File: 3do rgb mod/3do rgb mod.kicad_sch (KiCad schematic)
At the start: 12 parts

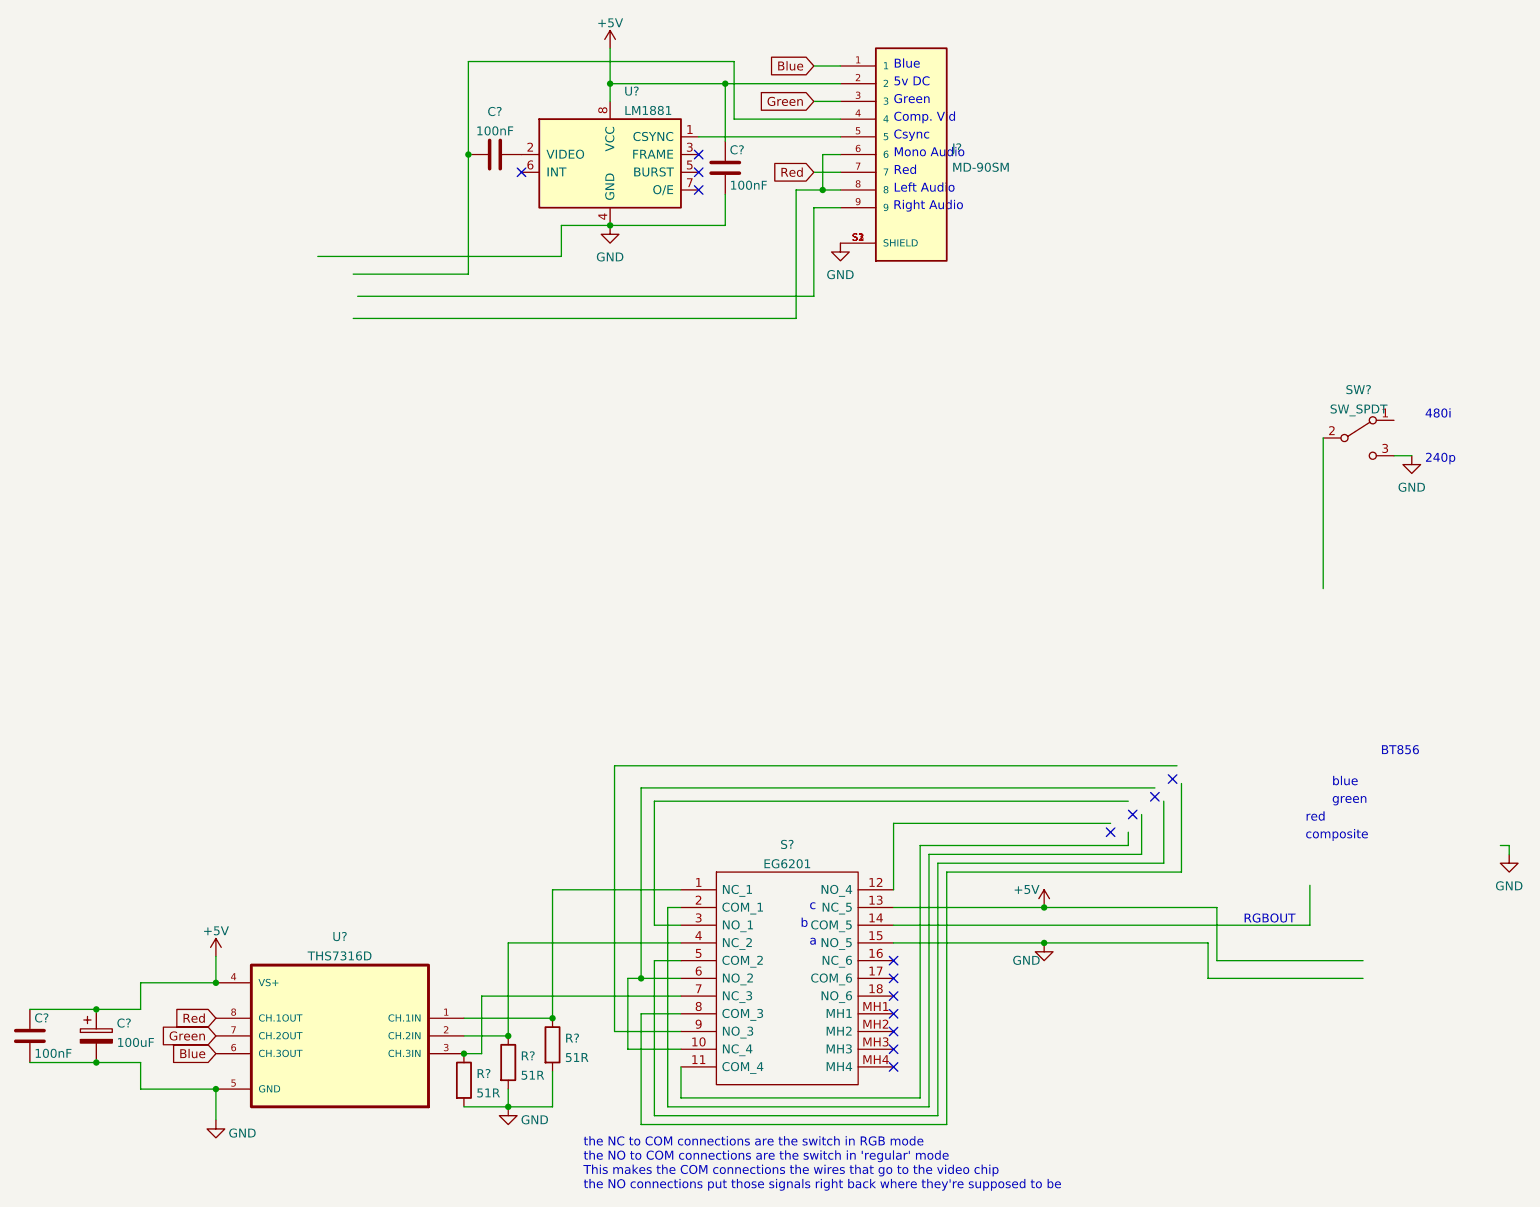
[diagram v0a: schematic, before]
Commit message: added scart cable pinout
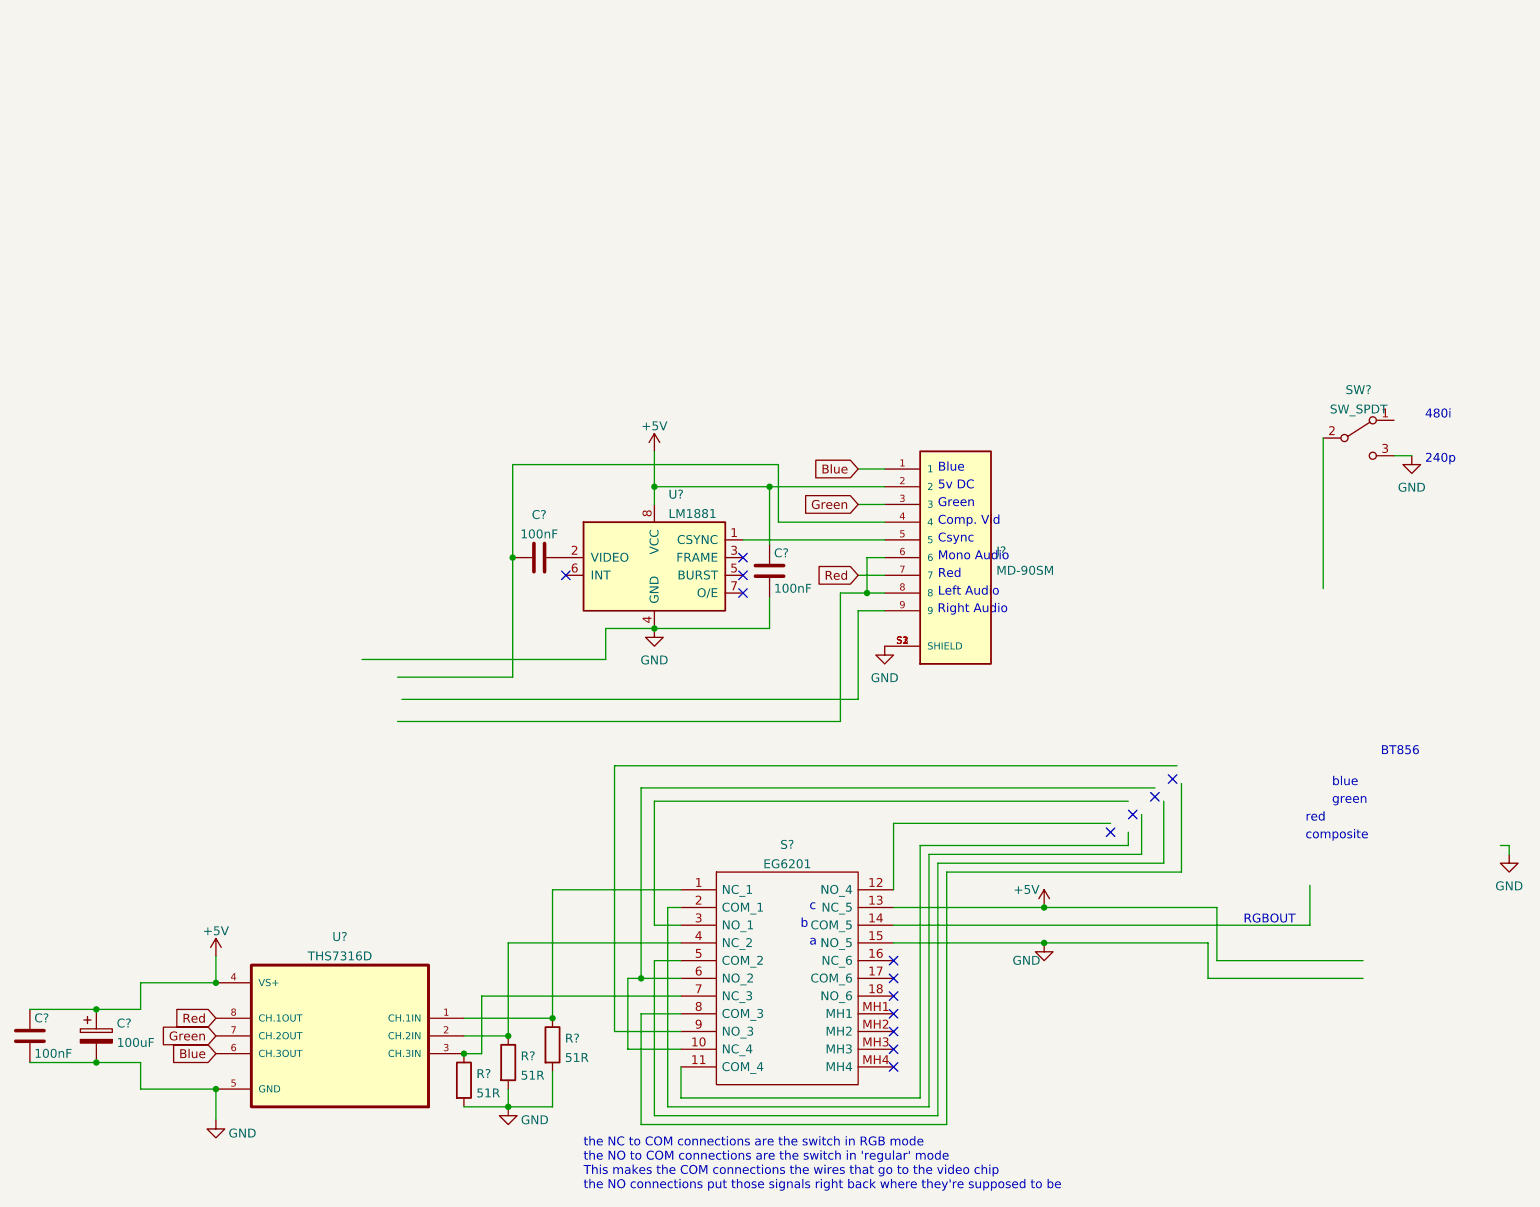
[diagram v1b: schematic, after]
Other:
- moved on the sheet: C?, J?, U?
